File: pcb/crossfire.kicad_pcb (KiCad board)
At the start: 4 copper layers, 100 x 80 mm, 144 parts, among them J1 SWD+UART, J2 USB_A, J3 USB_A, J4 USB_A, J5 USB_A, J6 USB-C data, J7 1S LiPo, J8 USB-C power, Q1 Q_Dual_NMOS_S1G1S2G2D2D2D1D1, Q2 Q_Dual_NMOS_S1G1S2G2D2D2D1D1, Q3 Q_Dual_NMOS_S1G1S2G2D2D2D1D1, SW1 BOOT, SW2 RESET, SW3 USER, U1 RP2350A, U10 TPS2065C, U11 USBLC6-2SC6, U12 USBLC6-2SC6, U13 BQ25798, U14 TPS63060, U15 TPS61089, U16 HUSB238, U17 RM2, U2 W25Q128JVS, U3 USB2514B, U4 TPS2065C, U5 USBLC6-2SC6, U6 TPS2065C, U7 USBLC6-2SC6, U8 TPS2065C, U9 USBLC6-2SC6, Y1 12MHz, Y2 24MHz

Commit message: place the passives beside the pins they serve, and the port clamps behind them
The 113 parts left parked are passives, and a passive's position is not a free choice: a decoupling
capacitor belongs at the pin it decouples, a divider at the pin it feeds, a load capacitor at the
crystal. Nearly all of that is already in the connection list, so it was read from there rather than
decided. For each part, a pad of an already-placed part sharing one of its nets is its anchor, and
the part sits as near it as there is room. Ground is excluded: every one of them touches it and
nothing is learned from that.

Two things the connection list does not say, both found by getting them wrong first. Which chip a
rail capacitor belongs to -- on the net list every 3.3V bypass is the same two nets, so the radio's
three and the converter's output bulk went to the hub, which happened to own the nearest pad on the
rail. The drawing does say, because a part is on the sheet of the block it serves, so the sheet now
comes first and all 113 ended up beside something on their own sheet. And that a pin can only have
one part next to it -- six capacitors anchored to the same hub pad and fanned out from it. A pad is
claimed once used, so six supply pins get their six bypasses one to a pin.

The four port clamps moved to the back of the board, which is the one placement decision here that
costs something. A clamp works by being nearer the pin than anything it protects, because what it has
to beat is the inductance of the track in front of it. On the front it cannot be near: the receptacle
is a horizontal through-hole part whose housing covers a strip 10mm deep inboard of its own pins, and
its data pins sit at the end of the row furthest from the only gap the 25.4mm pitch leaves. The best
front-side position is 11.5mm on three ports and 16.8mm on the fourth. Behind the housing the same
area is free and the pins are through-hole, so each clamp now sits 3.2mm from what it protects,
through the board rath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
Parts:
- U11, U5, U7, U9: moved to B.Cu
- moved C80 190.7 mm to (10.1, 61.0), turned to 90 degrees
- moved R47 185.3 mm to (12.6, 34.4)
- moved R58 176.1 mm to (20.0, 13.0)
- moved C69 174.7 mm to (22.9, 31.8), turned to 90 degrees
- moved C91 174.0 mm to (25.4, 57.9), turned to 90 degrees
- moved C78 173.6 mm to (4.11, 47.4)
- moved C67 171.0 mm to (13.3, 37.7), turned to 90 degrees
- moved R46 170.5 mm to (20.8, 32.2), turned to 90 degrees
- moved C68 169.5 mm to (21.5, 34.9)
- moved R57 168.6 mm to (20.2, 15.0)
- moved C90 166.3 mm to (25.4, 52.9), turned to 90 degrees
- moved C77 163.3 mm to (6.75, 41.2), turned to 90 degrees
- moved C79 162.5 mm to (21.9, 44.4), turned to 90 degrees
- moved R30 159.9 mm to (41.2, 10.9), turned to 90 degrees
- moved C40 159.4 mm to (23.2, 75.6)
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
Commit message: give the board four mounting holes, in the drawing as well as on it
They are in the schematic because everything else on this board is, and a part that exists only on
the board is one that quietly disappears the next time the board is rebuilt from the drawing. Being
there also means they carry a net, which they need: these are plated and bonded to ground. Bonded
rather than bare because the asymmetry favours it -- five connector shells are already at ground, so
a metal enclosure's screw should join that system deliberately rather than through whatever it
touches, and against a plastic one the bond costs nothing. Leaving the pads off is the version that
cannot be undone without a new board.

Where they go was not a choice. Three of the four corners are inside a part: the bottom edge is four
sockets on a fixed pitch spanning nearly the full width, and the top right is the radio's clearance,
which a screw and its standoff have to respect as much as copper does. The positions are the point
furthest from the middle of the board in each quarter where a fastener actually fits, taking 8mm of
clear diameter, because an M3 head is 5.5mm and a washer 7mm and a hole only the drill clears is one
that cannot be done up. The search is against the outline polygon and the rule areas rather than a
rectangle, after a first attempt answered with two positions that overhung the rounded corners and
one that sat 0.15mm from the antenna's clearance.

Two consequences belong to the enclosure and are recorded rather than hidden. There is no hole
position anywhere in the lower left, because the power section fills it. And nothing comes within
16mm of the socket row, which is exactly where a plug is pushed in, so the enclosure has to carry
that row on a ledge rather than rely on these four screws.

One bug of mine on the way, worth naming because it is the same one that produced seventy annotation
errors before: the new ground symbols were numbered by scanning the sheet being edited, and power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
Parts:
- added H1: MountingHole_3.2mm_M3_Pad, MountingHole_3.2mm_M3_Pad, F.Cu at (4.00, 6.50)
- added H2: MountingHole_3.2mm_M3_Pad, MountingHole_3.2mm_M3_Pad, F.Cu at (95.5, 14.5)
- added H3: MountingHole_3.2mm_M3_Pad, MountingHole_3.2mm_M3_Pad, F.Cu at (36.5, 59.5)
- added H4: MountingHole_3.2mm_M3_Pad, MountingHole_3.2mm_M3_Pad, F.Cu at (81.5, 59.5)

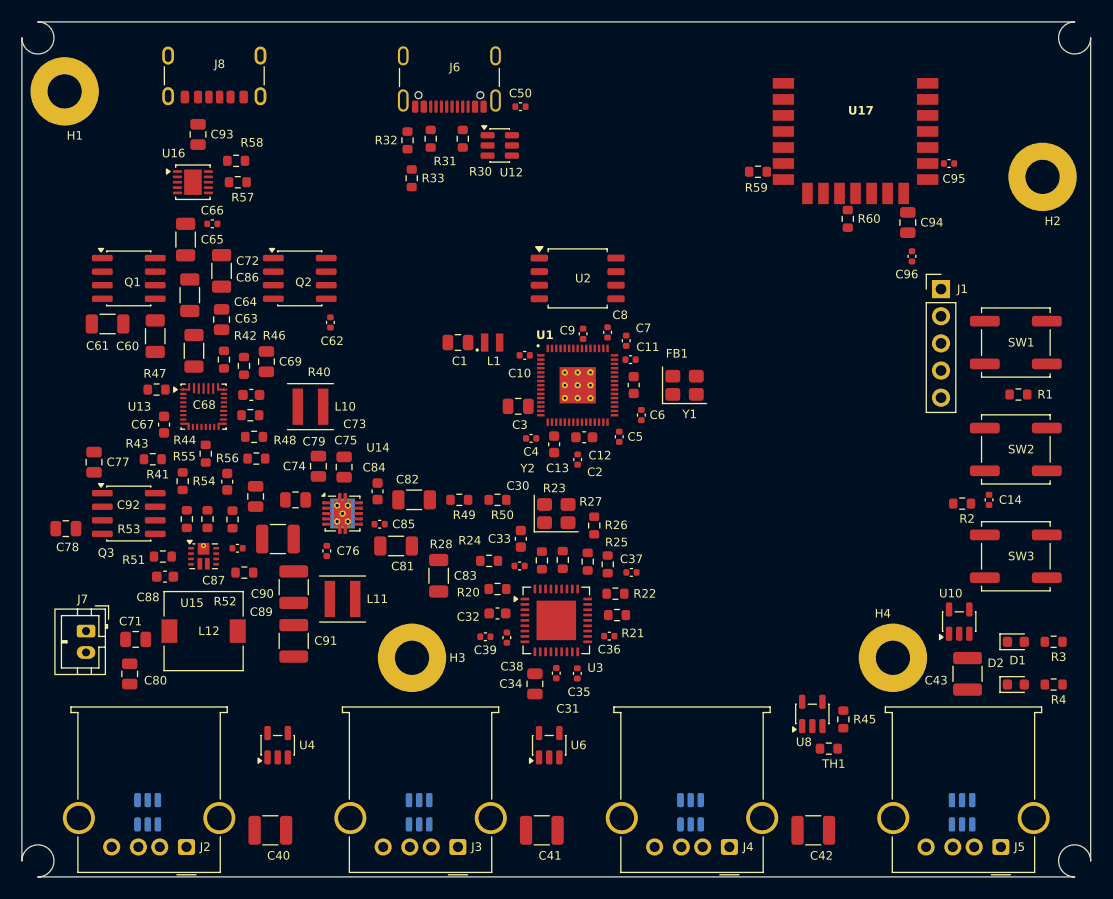
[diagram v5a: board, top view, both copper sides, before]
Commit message: pour the planes and stitch them, and turn sixty parts the right way round
Ground is one unbroken piece on the first inner layer, and is never divided. It is the reference the
pairs are routed over, and a return follows its own signal rather than the shortest path, so a slot
across it would push that return the long way round and turn a tidy pair into a loop.

The second inner layer carries the rails, split by current rather than by pin count. The system rail
is local -- the charger that makes it, the converters that draw on it, the cell and the ship switch
are one block on the left, and it carries the most current on the board over twenty millimetres. The
5 V rail is the long one, made at the boost and consumed at four port switches seventy millimetres
away, so it takes the bottom band, stepping up beyond x 78 where the fourth port's switch sits higher
than the other three. The 3.3 V rail takes the rest.

Those shapes are drawn to the pads, not guessed: a first attempt ran the 5 V band up to y 52 across
the full width, which put it under the hub and left that part's six supply pins with no 3.3 V plane
beneath them.

Fourteen pads deliberately sit over a neighbouring rail's plane, which is the right answer rather
than a defect. They are the two converters' own output clusters, standing inside the block that feeds
them; one inner layer cannot give both the input and the output of a converter copper in the same
square millimetre, so those nodes join on the surface and drop to their rail where the plane begins.
Checked rather than assumed: every system-rail pad is over its own plane, and no pad is over nothing.

Then the vertical connections. 94 ground stitching vias on an 8mm grid tie the two outer pours and
the inner plane into one piece of metal. Each rail pad gets a via and a stub, and the direction of
that stub is the whole problem: the first attempt took the nearest free position in any direction,
which on 0.4mm pitch means leaving a pad sideways across its neighb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
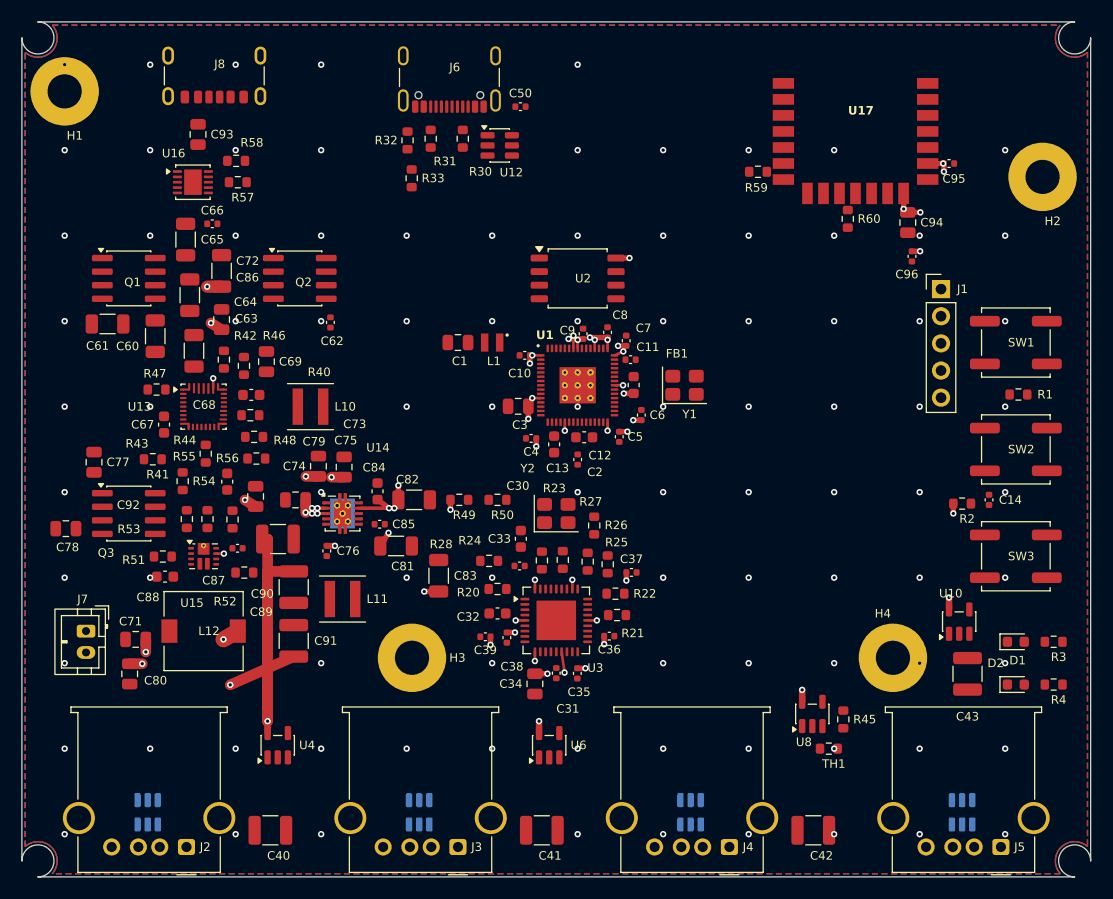
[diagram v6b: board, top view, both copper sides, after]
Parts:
- turned C1 to 180 degrees
- turned C10 to 180 degrees
- turned C13 to -90 degrees
- turned C14 to -90 degrees
- turned C2 to -90 degrees
- turned C3 to 180 degrees
- turned C32 to 180 degrees
- turned C33 to -90 degrees
- turned C34 to -90 degrees
- turned C35 to -90 degrees
- turned C38 to -90 degrees
- turned C39 to 180 degrees
- turned C4 to 180 degrees
- turned C40 to 180 degrees
- turned C41 to 180 degrees
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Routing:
- net +3V3: track 0.00 -> 48.8 mm, vias 0 -> 44
- net +5V: track 0.00 -> 45.0 mm, vias 0 -> 5
- net /power/VSYS: track 0.00 -> 17.5 mm, vias 0 -> 16
- net GND: vias 0 -> 93
- added copper zone on In2.Cu, net +3V3
- added copper zone on In2.Cu, net +5V
- added copper zone on In2.Cu, net /power/VSYS
- added copper zone on B.Cu, net GND
- added copper zone on F.Cu, net GND
- added copper zone on In1.Cu, net GND

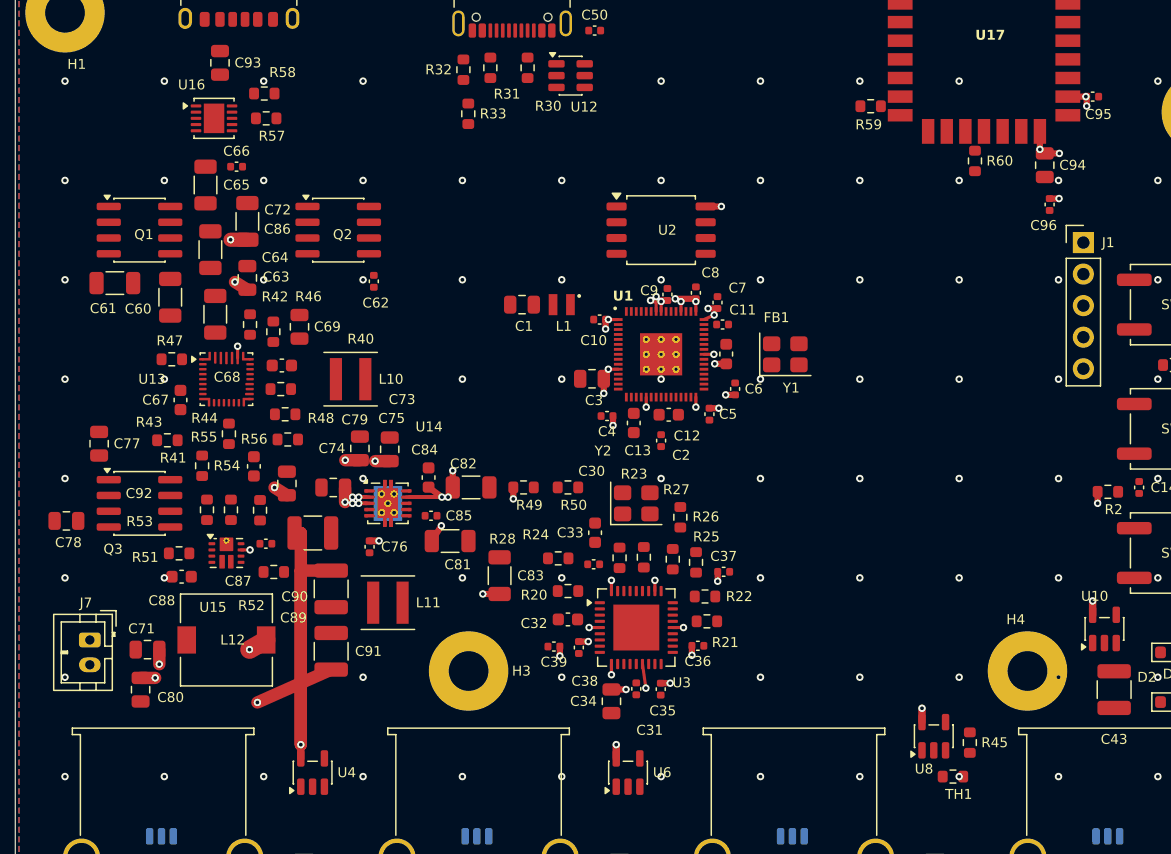
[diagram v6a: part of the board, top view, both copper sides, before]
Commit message: place the fast nodes by measurement, which halved every switch node and crystal
Listing the critical nets before routing them showed the problem was not routing. The charger's
switch node spanned 15.5mm, the core regulator's 10.7, the boost's 11.5, and both crystals about ten.
A switch node swings the full input voltage in nanoseconds and the loop it makes with its inductor
and input capacitor is the one that radiates; a crystal's two pins are the most sensitive input the
processor has. The area of those loops is set by where the parts are, and no amount of careful copper
between them fixes a part in the wrong place.

The cause was the first floorplan, which put the four power inductors and both crystals at positions
chosen by eye. The general placement rule did not correct it, because it places a part's CENTRE near
an anchor PAD and has no opinion about which of the part's own pads faces it. On a 7.3mm inductor
those are different questions: the boost's sat with its switch pad 13mm from the switch pin and its
output pad pointing back at the converter.

Those parts are no longer placed by eye or by the general rule. Each pad that shares a net with a
device pin is given that pin as a target, and the part is searched over all four orientations and
every position on a fine grid for the one minimising total distance to its own targets without
touching anything -- a measurement that can be argued with rather than a heuristic. They are also
placed FIRST, before the bypasses, because a pad is claimed once and whoever gets there takes it;
placing them after left a bootstrap capacitor at a switch pin with its inductor seven millimetres
out, and a load capacitor at a crystal pin with the crystal beyond it.

Across the ten nodes: 107.7mm of span originally, 46.6mm now. Pin to inductor is 0.9 to 6.8mm and
most are three to four. The same reasoning gave the general pass a tie-break it did not have -- when
an inductor, a capacitor and a resistor all want the same pin, they are no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
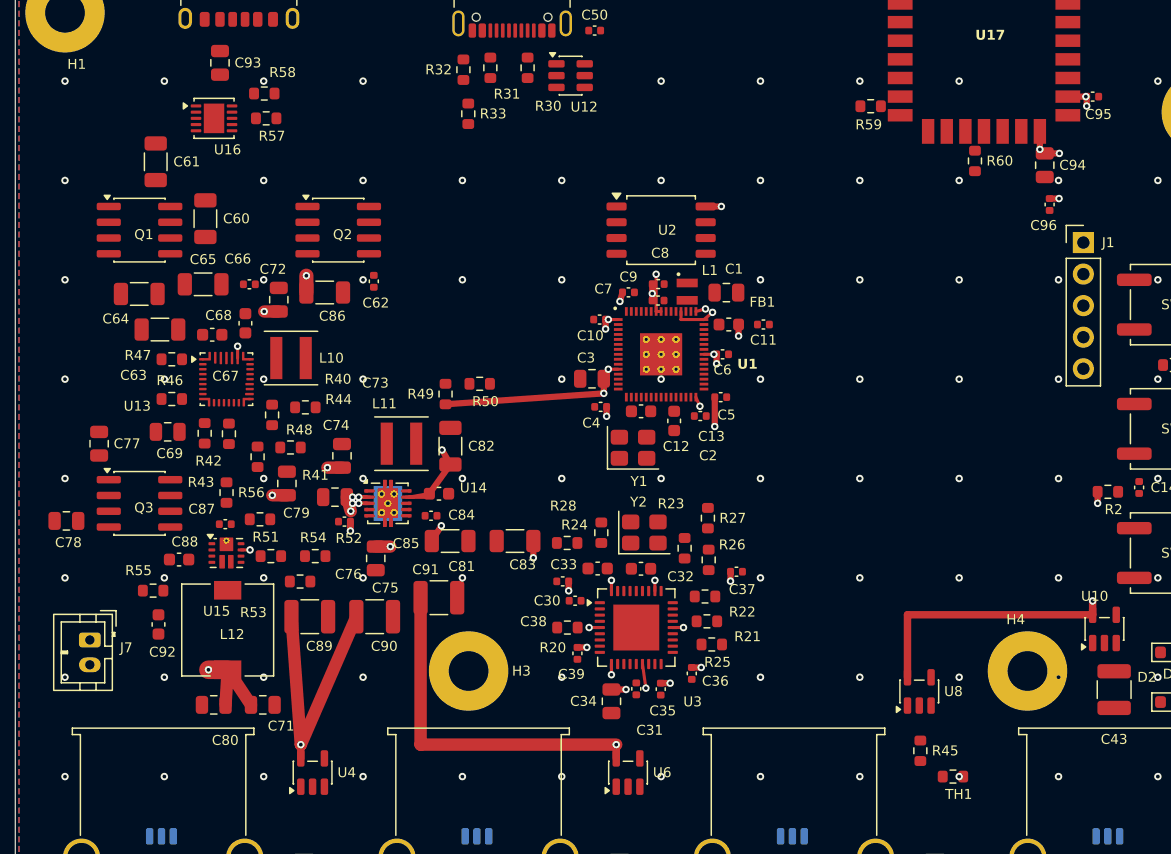
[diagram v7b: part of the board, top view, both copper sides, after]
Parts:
- moved C1 16.5 mm to (57.3, 29.0), turned to 0 degrees
- moved C92 14.9 mm to (11.5, 55.7)
- moved Y1 14.4 mm to (49.7, 41.5)
- moved C69 13.6 mm to (12.3, 40.2), turned to 0 degrees
- moved L11 12.9 mm to (31.1, 41.2)
- moved R54 11.7 mm to (24.1, 50.2), turned to 0 degrees
- moved R50 11.0 mm to (37.4, 36.4)
- moved C61 10.3 mm to (11.3, 18.5), turned to 90 degrees
- moved C71 10.3 mm to (19.9, 62.2), turned to 0 degrees
- moved L1 10.2 mm to (54.1, 29.0), turned to -90 degrees
- moved R41 9.93 mm to (22.2, 41.5), turned to 180 degrees
- moved R46 9.81 mm to (12.6, 37.6), turned to 180 degrees
- moved R49 9.80 mm to (34.6, 37.2), turned to 90 degrees
- moved C91 9.69 mm to (34.1, 53.6), turned to 180 degrees
- moved C66 9.53 mm to (18.8, 28.4)
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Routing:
- net +5V: track 45.0 -> 72.4 mm, vias 5 -> 3
- net +3V3: track 48.8 -> 62.2 mm, vias 44 -> 37
- net /power/VSYS: track 17.5 -> 21.4 mm, vias 16 -> 14
- net GND: vias 93 -> 98
